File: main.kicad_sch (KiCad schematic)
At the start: 46 parts, among them J16 Conn_01x01_Female, J17 Conn_01x03_Socket

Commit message: Added an input protection circuit Added CI
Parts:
- added G1: QR_Code, Custom_footprints_project:qr-code, symbol Custom_logos:QR_Code
- added LOGO2: Logo_RoHS, Symbol:RoHS-Logo_6mm_SilkScreen, symbol Custom_logos:Logo_RoHS
- H1, H42: DNP (none) -> 1
- H10: renamed from H19; DNP (none) -> 1
- H11: renamed from H21; DNP (none) -> 1
- H12: renamed from H23; DNP (none) -> 1
- H13: renamed from H25; DNP (none) -> 1
- H14: renamed from H27; DNP (none) -> 1
- H15: renamed from H29; DNP (none) -> 1
- H16: renamed from H31; DNP (none) -> 1
- H17: renamed from H33; DNP (none) -> 1
- H18: renamed from H35; DNP (none) -> 1
- H19: renamed from H37; DNP (none) -> 1
- H2: renamed from H3; DNP (none) -> 1
- H20: renamed from H39; DNP (none) -> 1
- H21: renamed from H41; DNP (none) -> 1
- H22: renamed from H2; DNP (none) -> 1
- H23: renamed from H4; DNP (none) -> 1
- H24: renamed from H6; DNP (none) -> 1
- H25: renamed from H8; DNP (none) -> 1
- H26: renamed from H10; DNP (none) -> 1
- H27: renamed from H12; DNP (none) -> 1
- H28: renamed from H14; DNP (none) -> 1
- H29: renamed from H16; DNP (none) -> 1
- H3: renamed from H5; DNP (none) -> 1
- H30: renamed from H18; DNP (none) -> 1
- H31: renamed from H20; DNP (none) -> 1
- H32: renamed from H22; DNP (none) -> 1
- H33: renamed from H24; DNP (none) -> 1
- H34: renamed from H26; DNP (none) -> 1
- H35: renamed from H28; DNP (none) -> 1
- H36: renamed from H30; DNP (none) -> 1
- H37: renamed from H32; DNP (none) -> 1
- H38: renamed from H34; DNP (none) -> 1
- H39: renamed from H36; DNP (none) -> 1
- H4: renamed from H7; DNP (none) -> 1
- H40: renamed from H38; DNP (none) -> 1
- H41: renamed from H40; DNP (none) -> 1
- H5: renamed from H9; DNP (none) -> 1
- H6: renamed from H11; DNP (none) -> 1
- H7: renamed from H13; DNP (none) -> 1
- H8: renamed from H15; DNP (none) -> 1
- H9: renamed from H17; DNP (none) -> 1
- J13: renamed from J16; Alternative Cliff FCR7350G -> Schützinger SWEB 8094 AU / GN (RoHS by excemption); MFN Schützinger -> Cliff; PN SWEB 8094 AU / GN -> FCR7350G; RoHS (none) -> Yes; Temperature (none) -> Tstorage = –25 °C to 80 °C, FCR7350G: -40 °C to 80 °C
- J14: renamed from J17; MFN Phoenix Contact -> Phoenix Contact|Phoenix Contact; PN 1924318 -> 1924318|1911978; RoHS (none) -> Yes; Temperature (none) -> Tstorage = –40 °C to 100 °C
- renumbered LOGO2 to LOGO3
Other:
- sheet Fischer renamed Fischer TFP
- sheet Fischer TFP: file fischer.kicad_sch -> fischer_TFP.kicad_sch
- note added: "Lead-free PCBs by PCBWay are compatible to RoHS 3 (EU Directive 2015/863). The certificate states RoHS-2 compatibility and were additionally tested according to IEC 62321-8:2017 for Phthalates (DBP, BBP, DEHP, DIBP) -> RoHS-3"
- note added: "Note: The Design can withstand +-40 V on each (!) pin. Increase clearance of the unprotected nets to 0.3 mm"
- note added: "The backplane has 6 slots. The typical input capacitance of devices: - Old style laser current driver is: 300 µF - HTC1500 temperature controller: 250 µF"

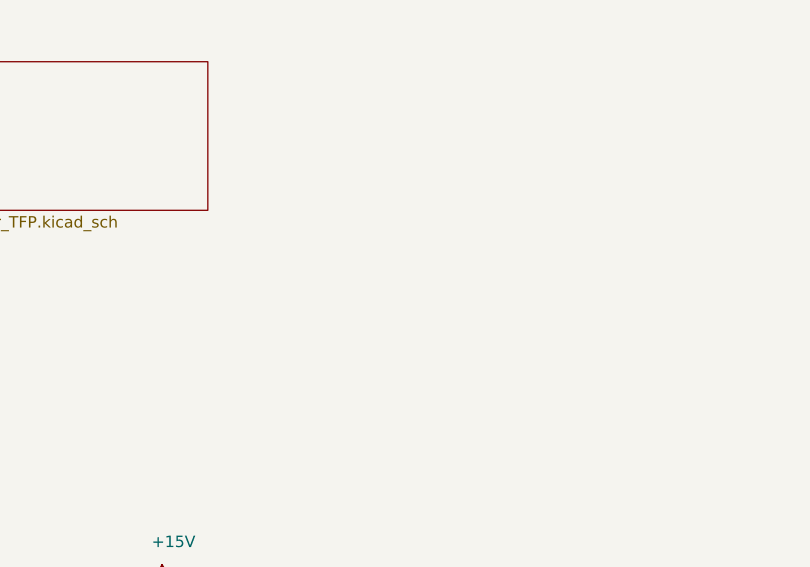
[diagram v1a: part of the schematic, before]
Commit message: Added Ferrite beads at the board input Moved power connector silkscreen labels Added TODO list for v.2.1.0
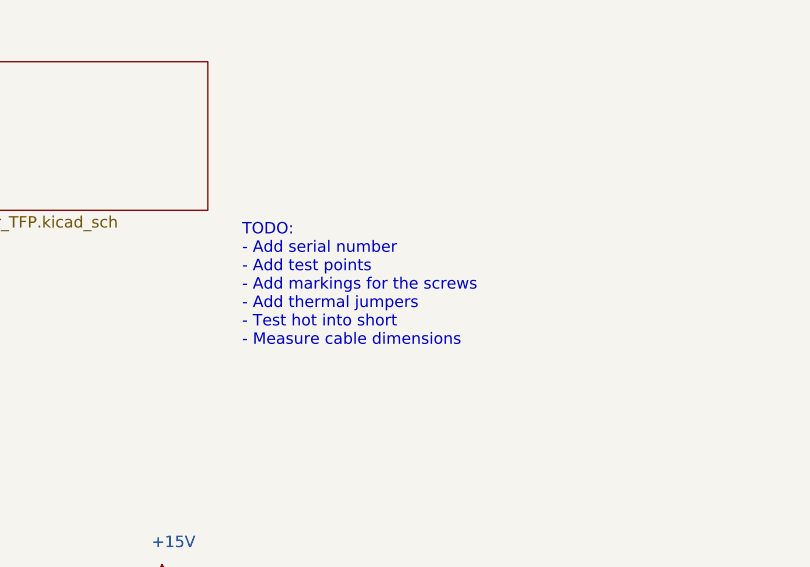
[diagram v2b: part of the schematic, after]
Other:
- note added: "TODO: - Add serial number - Add test points - Add markings for the screws - Add thermal jumpers - Test hot into short - Measure cable dimensions"
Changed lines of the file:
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@@
+    (effects (font (size 1.27 1.27)) (justify left bottom))
+  )
+  (text "TODO:\n- Add serial number\n- Add test points\n- Add markings for the screws\n- Add thermal jumpers\n- Test hot into short\n- Measure cable dimensions"
+    (at 109.22 57.15 0)
     (effects (font (size 1.27 1.27)) (justify left bottom))
   )

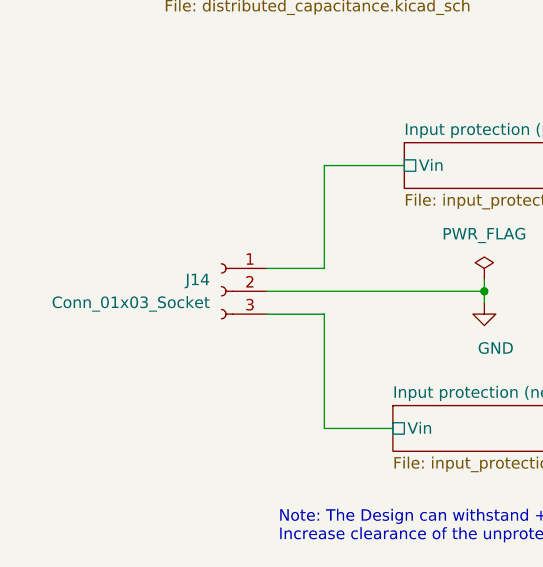
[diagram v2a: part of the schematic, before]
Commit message: Changed PCB connector to right angled variant Moved all components to the top side
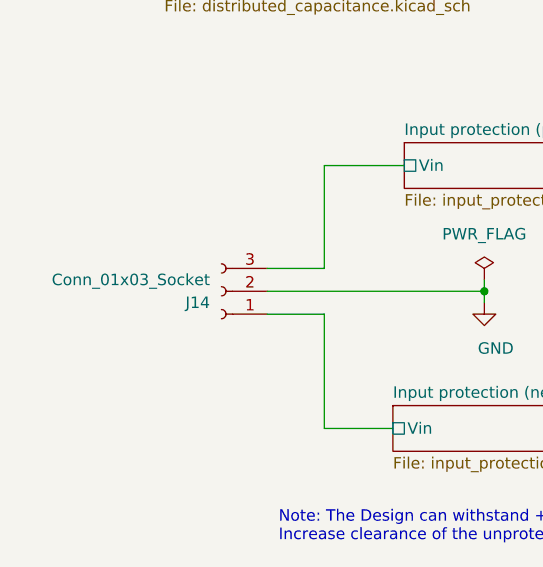
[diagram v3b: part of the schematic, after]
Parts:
- J14: footprint Connector_Phoenix_MSTB:PhoenixContact_MSTBVA_2,5_3-G-5,08_1x03_P5.08mm_Vertical -> Connector_Phoenix_MSTB:PhoenixContact_MSTBA_2,5_3-G-5,08_1x03_P5.08mm_Horizontal; PN 1924318|1911978 -> 1923872|1911978
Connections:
- net Input protection (negative)/Vin: now also J14.1 (Pin_1); no longer J14.3 (Pin_3)
- net Input protection (postive)/Vin: now also J14.3 (Pin_3); no longer J14.1 (Pin_1)
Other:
- moved on the sheet: J14
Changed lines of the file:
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@@
     )
   )
-  (symbol (lib_id "Connector:Conn_01x03_Socket") (at 38.1 102.87 0) (mirror y) (unit 1)
+  (symbol (lib_id "Connector:Conn_01x03_Socket") (at 38.1 102.87 180) (unit 1)
     (in_bom yes) (on_board yes) (dnp no)
-    (property "Reference" "J14" (at 36.83 101.6 0)
+    (property "Reference" "J14" (at 36.83 104.14 0)
       (effects (font (size 1.27 1.27)) (justify left))
     )
-    (property "Value" "Conn_01x03_Socket" (at 36.83 104.14 0)
+    (property "Value" "Conn_01x03_Socket" (at 36.83 101.6 0)
       (effects (font (size 1.27 1.27)) (justify left))
     )
-    (property "Footprint" "Connector_Phoenix_MSTB:PhoenixContact_MSTBVA_2,5_3-G-5,08_1x03_P5.08mm_Vertical" (at 38.1 102.87 0)
+    (property "Footprint" "Connector_Phoenix_MSTB:PhoenixContact_MSTBA_2,5_3-G-5,08_1x03_P5.08mm_Horizontal" (at 38.1 102.87 0)
       (effects (font (size 1.27 1.27)) hide)
     )
@@
       (effects (font (size 1.27 1.27)) hide)
     )
-    (property "PN" "1924318|1911978" (at 38.1 102.87 0)
+    (property "PN" "1923872|1911978" (at 38.1 102.87 0)
       (effects (font (size 1.27 1.27)) hide)
     )

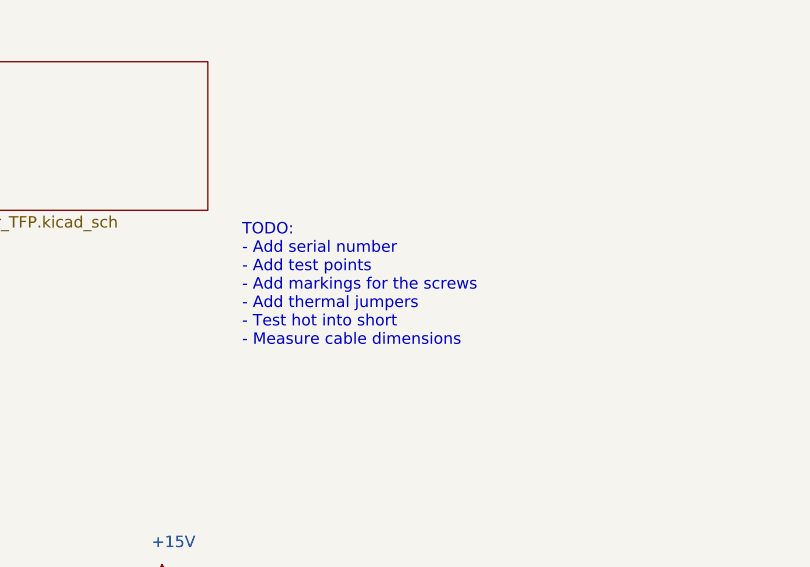
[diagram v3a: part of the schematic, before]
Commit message: Replace negative rail NMOS with SQJQ160E to reduce the on resistance
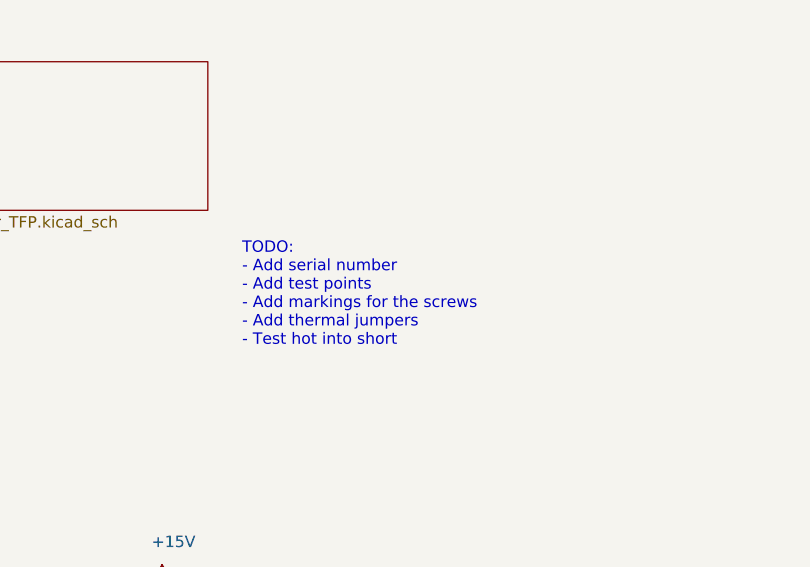
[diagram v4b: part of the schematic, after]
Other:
- note added: "TODO: - Add serial number - Add test points - Add markings for the screws - Add thermal jumpers - Test hot into short"
- note removed: "TODO: - Add serial number - Add test points - Add markings for the screws - Add thermal jumpers - Test hot into short - Measure cable dimensions"
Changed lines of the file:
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@@
     (effects (font (size 1.27 1.27)) (justify left bottom))
   )
-  (text "TODO:\n- Add serial number\n- Add test points\n- Add markings for the screws\n- Add thermal jumpers\n- Test hot into short\n- Measure cable dimensions"
+  (text "TODO:\n- Add serial number\n- Add test points\n- Add markings for the screws\n- Add thermal jumpers\n- Test hot into short"
     (at 109.22 57.15 0)
     (effects (font (size 1.27 1.27)) (justify left bottom))

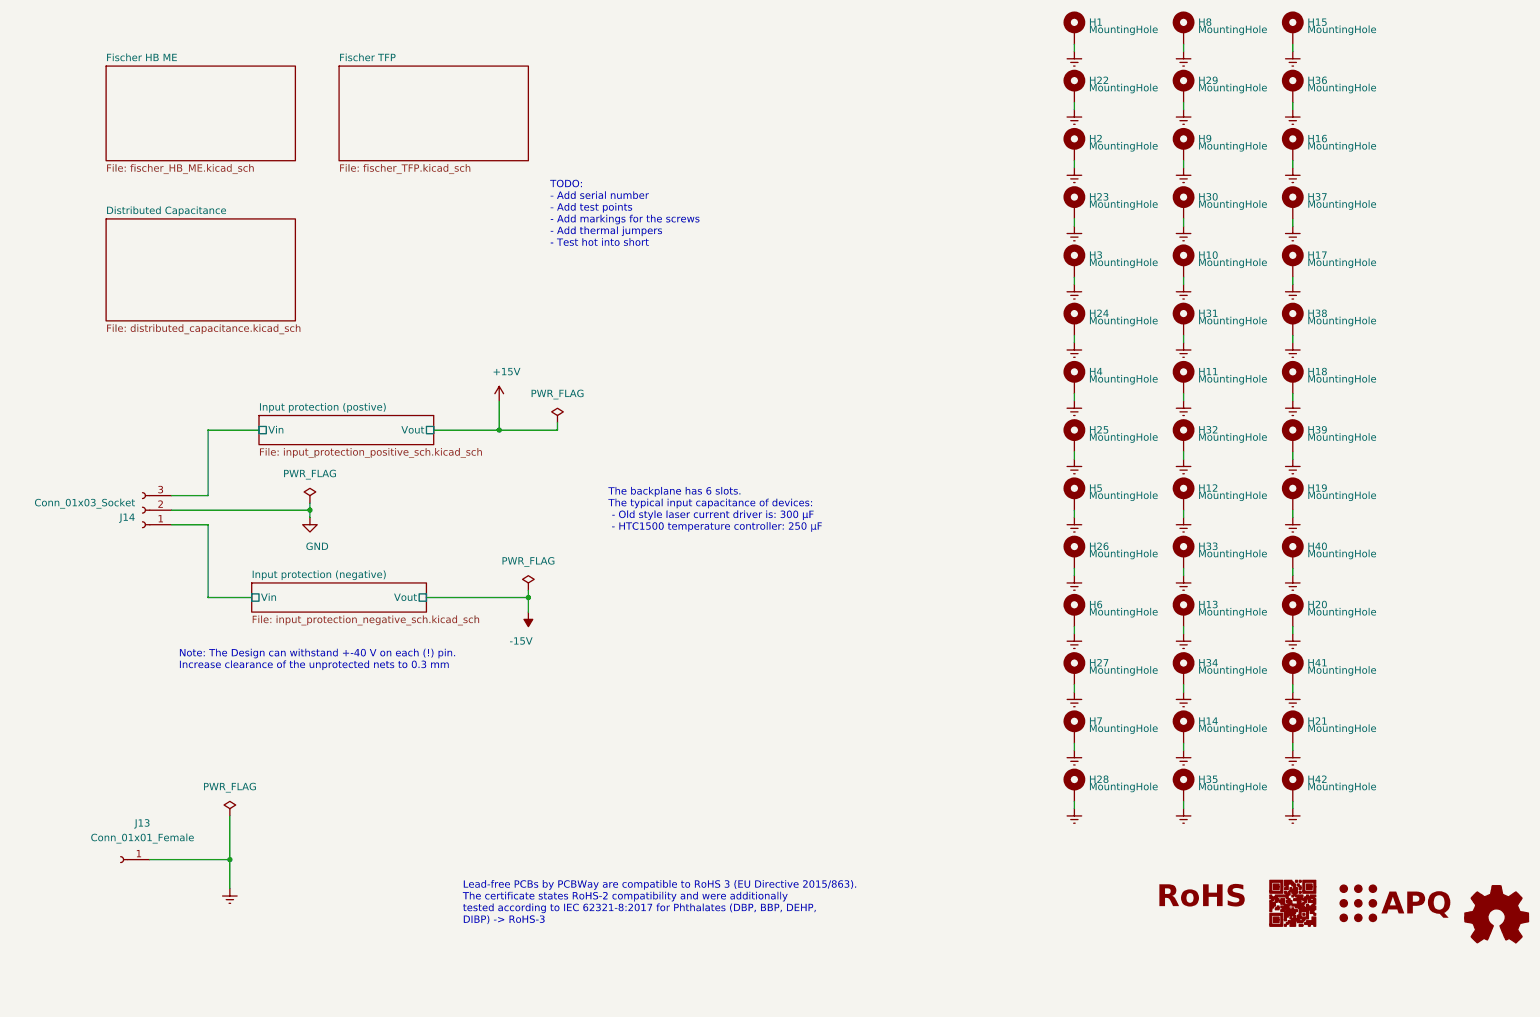
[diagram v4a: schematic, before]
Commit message: Updated board dimensions and location of connectors to match IEEE 1101.1-1991 Added markings for the mounting screws
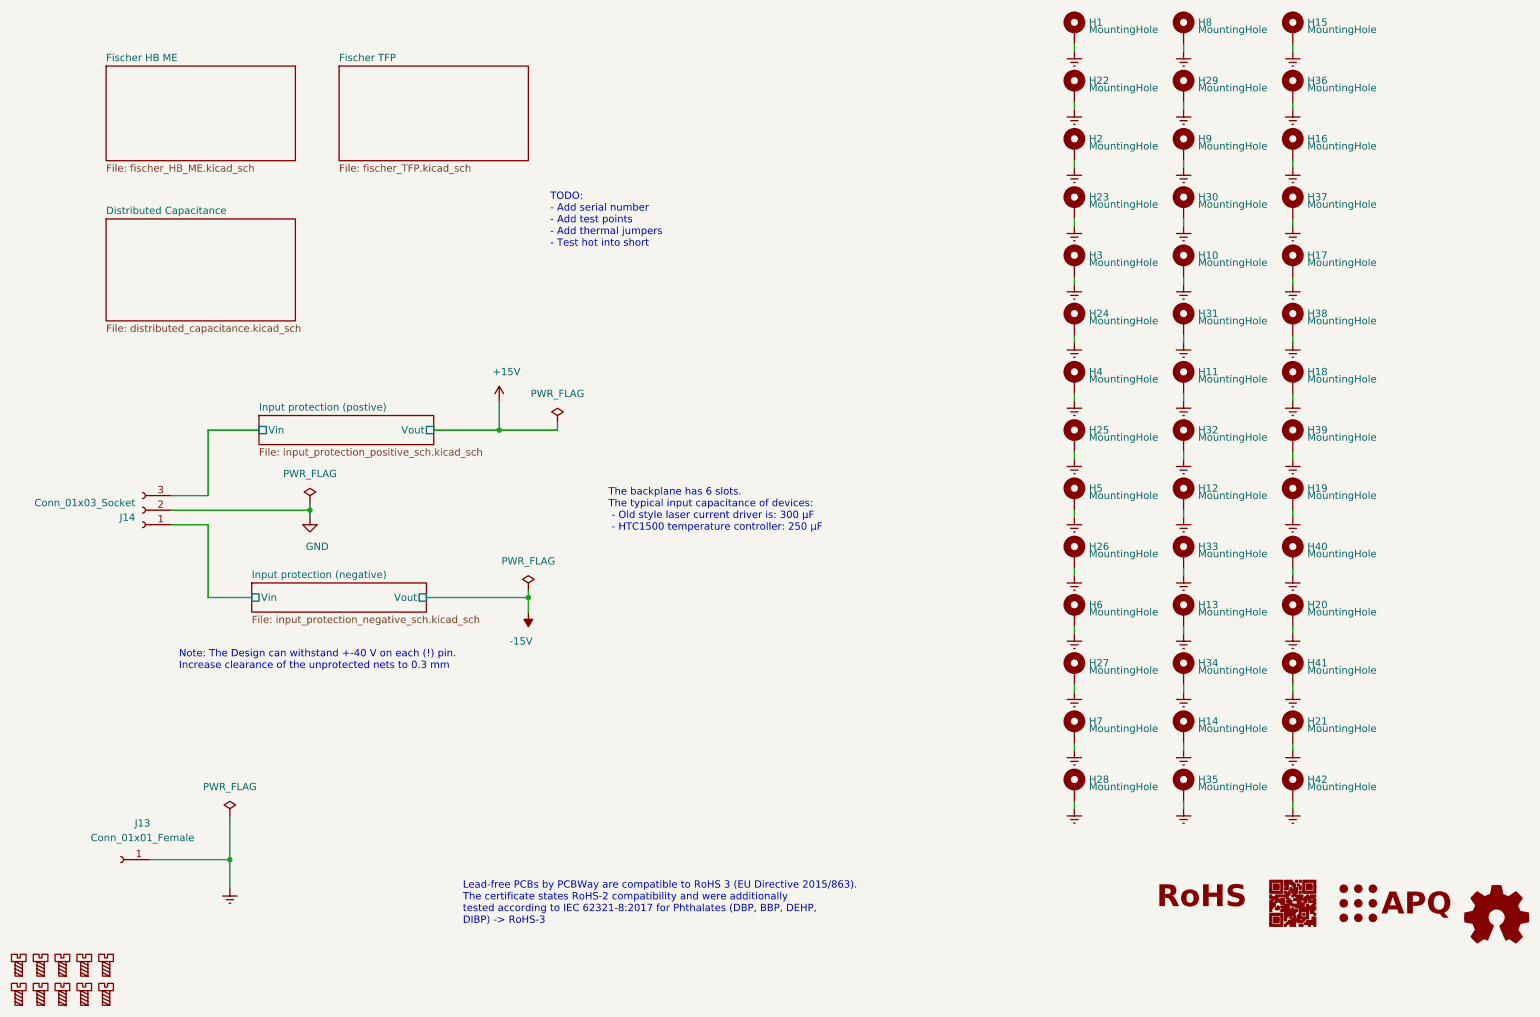
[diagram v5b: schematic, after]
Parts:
- added SYM1, SYM10, SYM2, SYM3, SYM4, SYM5, SYM6, SYM7, SYM8, SYM9: SYM_Screw, Custom_footprints:Symbol_screw, symbol Custom_logos:SYM_Screw
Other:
- note added: "TODO: - Add serial number - Add test points - Add thermal jumpers - Test hot into short"
- note removed: "TODO: - Add serial number - Add test points - Add markings for the screws - Add thermal jumpers - Test hot into short"

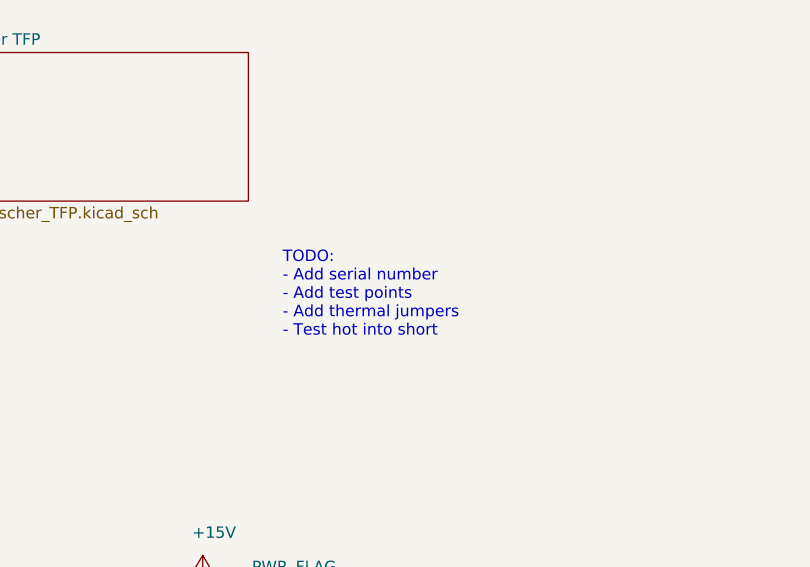
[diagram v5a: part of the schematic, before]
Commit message: Added thermal jumpers Increased copper area at the PMOS and the current sense resistors
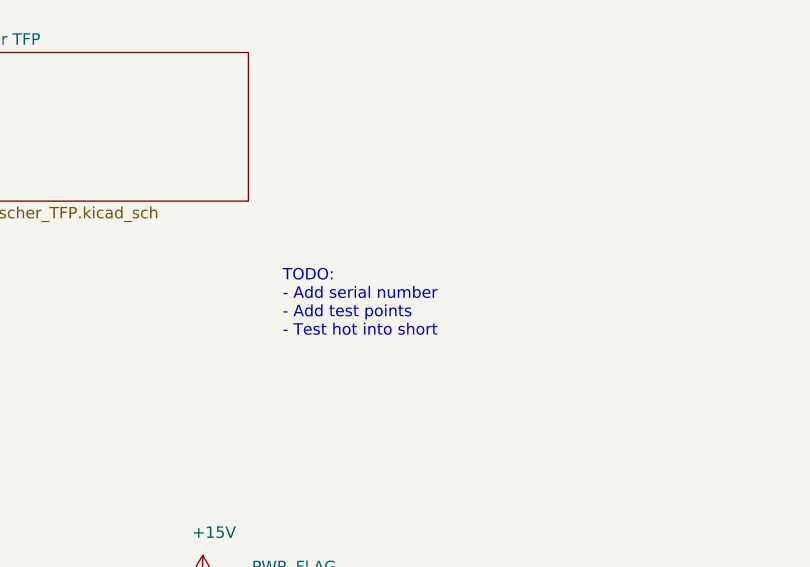
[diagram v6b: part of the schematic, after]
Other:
- note added: "TODO: - Add serial number - Add test points - Test hot into short"
- note removed: "TODO: - Add serial number - Add test points - Add thermal jumpers - Test hot into short"
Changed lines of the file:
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@@
     (effects (font (size 1.27 1.27)) (justify left bottom))
   )
-  (text "TODO:\n- Add serial number\n- Add test points\n- Add thermal jumpers\n- Test hot into short"
+  (text "TODO:\n- Add serial number\n- Add test points\n- Test hot into short"
     (at 109.22 57.15 0)
     (effects (font (size 1.27 1.27)) (justify left bottom))
